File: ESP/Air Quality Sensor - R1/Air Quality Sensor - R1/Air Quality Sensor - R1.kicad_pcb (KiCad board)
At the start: 2 copper layers, 101.6 x 76.2 mm, 27 parts, among them U1 SCD4X, U2 CCS811, U3 SGP40, U4 Sensair_Sunrise_006-0-0007, U5 MICS-VZ-89TE‎, U6 SCD30, U7 BME680

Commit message: Pile of uncommitted boards.
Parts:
- added C11: 0.1u, Capacitor_SMD:C_0603_1608Metric, F.Cu at (78.2, -53.6)
- added D1: LED, custom:CHIPLED_0603, F.Cu at (89.0, -3.00)
- added H1: MountingHole, MountingHole:MountingHole_3.2mm_M3_Pad_Via, F.Cu at (3.81, -78.7)
- added H2: MountingHole, MountingHole:MountingHole_3.2mm_M3_Pad_Via, F.Cu at (97.8, -78.7)
- added H3: MountingHole, MountingHole:MountingHole_3.2mm_M3_Pad_Via, F.Cu at (3.81, -3.81)
- added H4: MountingHole, MountingHole:MountingHole_3.2mm_M3_Pad_Via, F.Cu at (97.8, -3.81)
- added J1: Conn_01x05, Connector_JST:JST_XH_B3B-XH-AM_1x03_P2.50mm_Vertical, F.Cu at (59.7, -4.33)
- added J2: Conn_01x09, Connector_JST:JST_XH_B9B-XH-AM_1x09_P2.50mm_Vertical, F.Cu at (33.3, -4.45)
- added J3: Conn_01x05, Connector_JST:JST_XH_B5B-XH-AM_1x05_P2.50mm_Vertical, F.Cu at (71.2, -4.33)
- added J4: Conn_01x04, Connector_JST:JST_XH_B4B-XH-AM_1x04_P2.50mm_Vertical, F.Cu at (19.4, -4.45)
- added R10: 4.7K, Resistor_SMD:R_0603_1608Metric, F.Cu at (75.0, -13.4)
- added R11: 4.7K, Resistor_SMD:R_0603_1608Metric, F.Cu at (77.5, -13.4)
- added R12: 470R, Resistor_SMD:R_0603_1608Metric, F.Cu at (70.0, -13.5)
- added R13: 4.7K, Resistor_SMD:R_0603_1608Metric, F.Cu at (59.7, -30.5)
- added R14: 470R, Resistor_SMD:R_0603_1608Metric, F.Cu at (38.7, -11.4)
- added R6: 4.7K, Resistor_SMD:R_0603_1608Metric, F.Cu at (69.8, -30.8)
- added R7: 4.7K, Resistor_SMD:R_0603_1608Metric, F.Cu at (77.4, -30.8)
- added R8: 4.7K, Resistor_SMD:R_0603_1608Metric, F.Cu at (64.7, -30.8)
- added R9: 4.7K, Resistor_SMD:R_0603_1608Metric, F.Cu at (67.2, -30.8)
- added TP10: TestPoint_Small, Connector_Pin:Pin_D1.0mm_L10.0mm, F.Cu at (66.0, -74.9)
- added TP6: TestPoint_Small, Connector_Pin:Pin_D1.0mm_L10.0mm, F.Cu at (66.0, -64.8)
- added TP7: TestPoint_Small, Connector_Pin:Pin_D1.0mm_L10.0mm, F.Cu at (66.0, -69.8)
- added TP8: TestPoint_Small, Connector_Pin:Pin_D1.0mm_L10.0mm, F.Cu at (66.0, -54.6)
- added TP9: TestPoint_Small, Connector_Pin:Pin_D1.0mm_L10.0mm, F.Cu at (66.0, -59.7)
- added U8: ESP32-POE, custom:ESP32-POE, F.Cu at (101.6, -21.6)
- C2, C7: value 0.1u -> 1.0u
- C4, C9: value 1.0u -> 0.1u
- U1: value SCD4X -> CCS811; footprint Sensor_Gas:Sensirion_SCD4X_QFN-20_EP_10.1x10.1_Pitch1.25mm -> Package_LGA:AMS_LGA-10-1EP_2.7x4mm_P0.6mm
- U2: value CCS811 -> SGP40; footprint Package_LGA:AMS_LGA-10-1EP_2.7x4mm_P0.6mm -> Sensor_Gas:Sensirion_DFN-6-1EP_2.44x2.44mm_P0.8mm
- U3: value SGP40 -> SCD4X; footprint Sensor_Gas:Sensirion_DFN-6-1EP_2.44x2.44mm_P0.8mm -> Sensor_Gas:Sensirion_SCD4X_QFN-20_EP_10.1x10.1_Pitch1.25mm
- U5: value MICS-VZ-89TE‎ -> BME680; footprint Sensor_Gas:Telaire_MICS-VZ-89TE‎ -> Package_LGA:Bosch_LGA-8_3x3mm_P0.8mm_ClockwisePinNumbering
- U6: value SCD30 -> MICS-VZ-89TE‎; footprint Sensor_Gas:Sensiron_SCD30_Module -> Sensor_Gas:Telaire_MICS-VZ-89TE‎
- U7: value BME680 -> SCD30; footprint Package_LGA:Bosch_LGA-8_3x3mm_P0.8mm_ClockwisePinNumbering -> Sensor_Gas:Sensiron_SCD30_Module
- moved U5 262.0 mm to (6.99, -67.3), turned to 0 degrees
- moved R4 261.6 mm to (10.8, -69.3), turned to 180 degrees
- moved C6 259.6 mm to (5.33, -64.8), turned to 180 degrees
- moved R3 258.7 mm to (10.8, -66.3), turned to 180 degrees
- moved C5 256.4 mm to (8.37, -64.8), turned to 0 degrees
- moved C4 253.9 mm to (5.52, -57.7)
- moved U3 245.8 mm to (7.55, -50.9)
- moved C3 238.4 mm to (5.52, -44.0)
- moved TP3 220.6 mm to (42.5, -57.3)
- moved U7 220.6 mm to (40.6, -46.9)
- moved TP4 219.6 mm to (42.7, -61.0)
- moved C7 219.5 mm to (42.8, -48.3), turned to 0 degrees
- moved R5 217.7 mm to (42.8, -63.5), turned to 0 degrees
- moved R1 195.7 mm to (89.4, -45.0)
- moved U1 194.6 mm to (90.2, -48.3), turned to 90 degrees
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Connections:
- U1 pad 1: (no net) -> GND
- U1 pad 10: /SENS/SDA -> /SENS/SCL_2
- U1 pad 11: (no net) -> GND
- U1 pad 2: (no net) -> Net-(R1-Pad2)
- U1 pad 3: (no net) -> Net-(TP1-Pad1)
- U1 pad 4: (no net) -> Net-(U1-Pad4)
- U1 pad 5: (no net) -> Net-(U1-Pad4)
- U1 pad 6: GND -> +3V3
- U1 pad 7: +3V3 -> Net-(R2-Pad1)
- U1 pad 8: (no net) -> unconnected-(U1-Pad8)
- U1 pad 9: /SENS/SCL -> /SENS/SDA_2
- U2 pad 1: GND -> +3V3
- U2 pad 2: Net-(R1-Pad2) -> GND
- U2 pad 3: Net-(TP1-Pad1) -> /SENS/SDA_2
- U2 pad 4: Net-(U2-Pad4) -> unconnected-(U2-Pad4)
- U2 pad 5: Net-(U2-Pad4) -> +3V3
- U2 pad 6: +3V3 -> /SENS/SCL_2
- U2 pad 7: Net-(R2-Pad1) -> GND
- U3 pad 1: +3V3 -> (no net)
- U3 pad 2: GND -> (no net)
- U3 pad 3: /SENS/SDA -> (no net)
- U3 pad 4: unconnected-(U3-Pad4) -> (no net)
- U3 pad 5: +3V3 -> (no net)
- U3 pad 6: /SENS/SCL -> GND
- U3 pad 7: GND -> +3V3
- U4 pad 4: /SENS/SDA -> /SENS/SDA_1
- U4 pad 5: /SENS/SCL -> /SENS/SCL_1
- U4 pad 7: Net-(TP2-Pad1) -> Net-(TP5-Pad1)
- U5 pad 1: Net-(TP3-Pad1) -> GND
- U5 pad 2: /SENS/SCL -> Net-(R4-Pad2)
- U5 pad 3: GND -> /SENS/SDA_1
- U5 pad 4: /SENS/SDA -> /SENS/SCL_1
- U5 pad 5: unconnected-(U5-Pad5) -> Net-(R3-Pad2)
- U6 pad 1: +3V3 -> Net-(TP2-Pad1)
- U6 pad 2: GND -> /SENS/SCL_2
- U6 pad 3: /SENS/SCL -> GND
- U6 pad 4: /SENS/SDA -> /SENS/SDA_2
- U6 pad 5: Net-(TP4-Pad1) -> unconnected-(U6-Pad5)
- U6 pad 6: Net-(TP5-Pad1) -> +3V3
- U7 pad 1: GND -> +3V3
- U7 pad 2: Net-(R4-Pad2) -> GND
- U7 pad 3: /SENS/SDA -> /SENS/SCL_1
- U7 pad 4: /SENS/SCL -> /SENS/SDA_1
- U7 pad 5: Net-(R3-Pad2) -> Net-(TP3-Pad1)
- U7 pad 6: +3V3 -> Net-(TP4-Pad1)
- U7 pad 7: GND -> Net-(R5-Pad1)
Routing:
- net /SENS/SDA_1: track 0.00 -> 197.9 mm, vias 0 -> 3
- net /SENS/SCL_1: track 0.00 -> 186.9 mm, vias 0 -> 4
- net /SENS/SCL_2: track 0.00 -> 149.5 mm, vias 0 -> 4
- net /SENS/SDA_2: track 0.00 -> 134.1 mm
- net +5V: track 0.00 -> 81.7 mm, vias 0 -> 1
- net GND: track 0.00 -> 65.4 mm, vias 0 -> 20
- net Net-(J1-Pad2): track 0.00 -> 59.7 mm
- net Net-(R13-Pad1): track 0.00 -> 58.8 mm
- net +3V3: track 0.00 -> 55.3 mm, vias 0 -> 18
- net Net-(J2-Pad7): track 0.00 -> 54.8 mm, vias 0 -> 2
- net Net-(D1-Pad2): track 0.00 -> 32.6 mm
- net Net-(R14-Pad1): track 0.00 -> 17.7 mm
- net Net-(TP5-Pad1): track 0.00 -> 11.7 mm
- net Net-(J3-Pad3): track 0.00 -> 8.81 mm
- net Net-(J3-Pad4): track 0.00 -> 8.79 mm
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- added copper zone on In2.Cu, net +3V3
- added copper zone on In1.Cu, net GND
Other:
- board size 101.6 x 76.2 mm -> 101.6 x 82.5 mm
- copper layers 2 -> 4
- board text added: "GND"
- board text added: "SCL1"
- board text added: "SCL2"
- board text added: "SDA1"
- board text added: "SDA2"

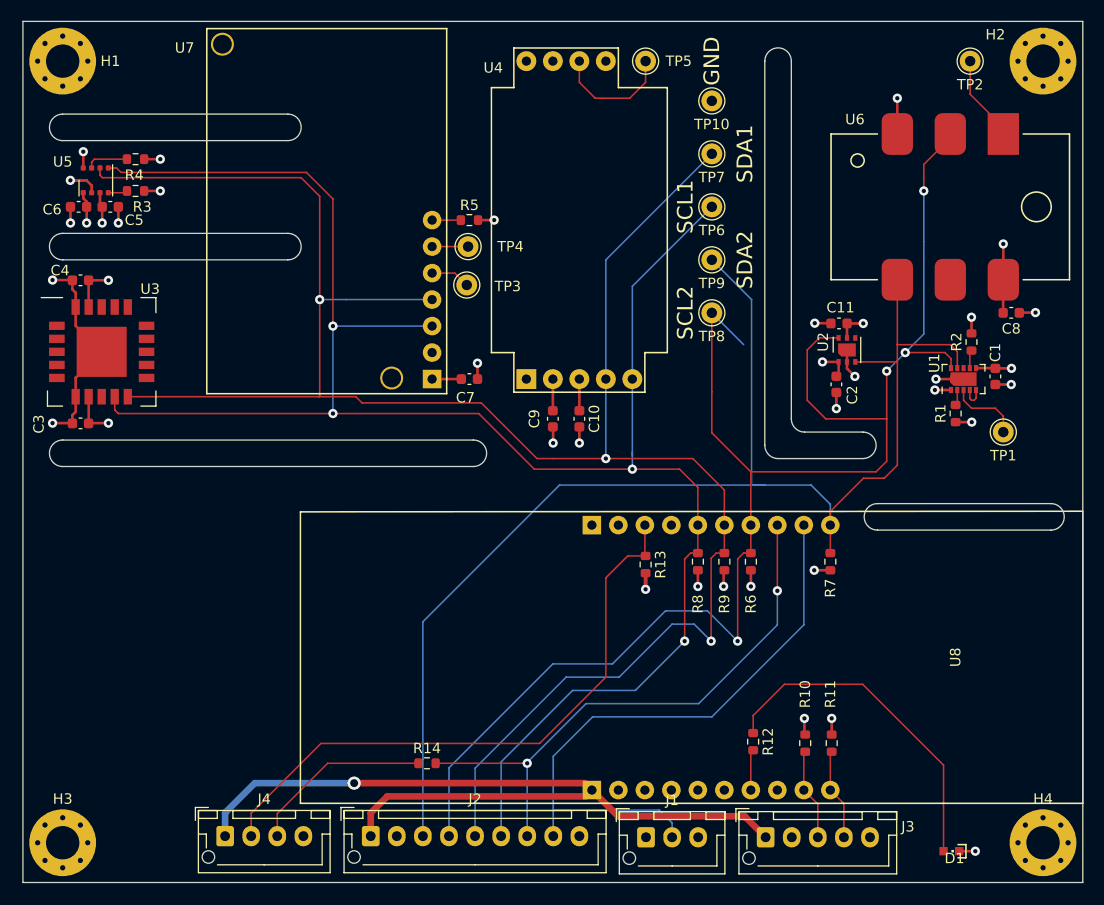
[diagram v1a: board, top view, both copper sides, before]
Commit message: Reworking things to use the new controller PCB.
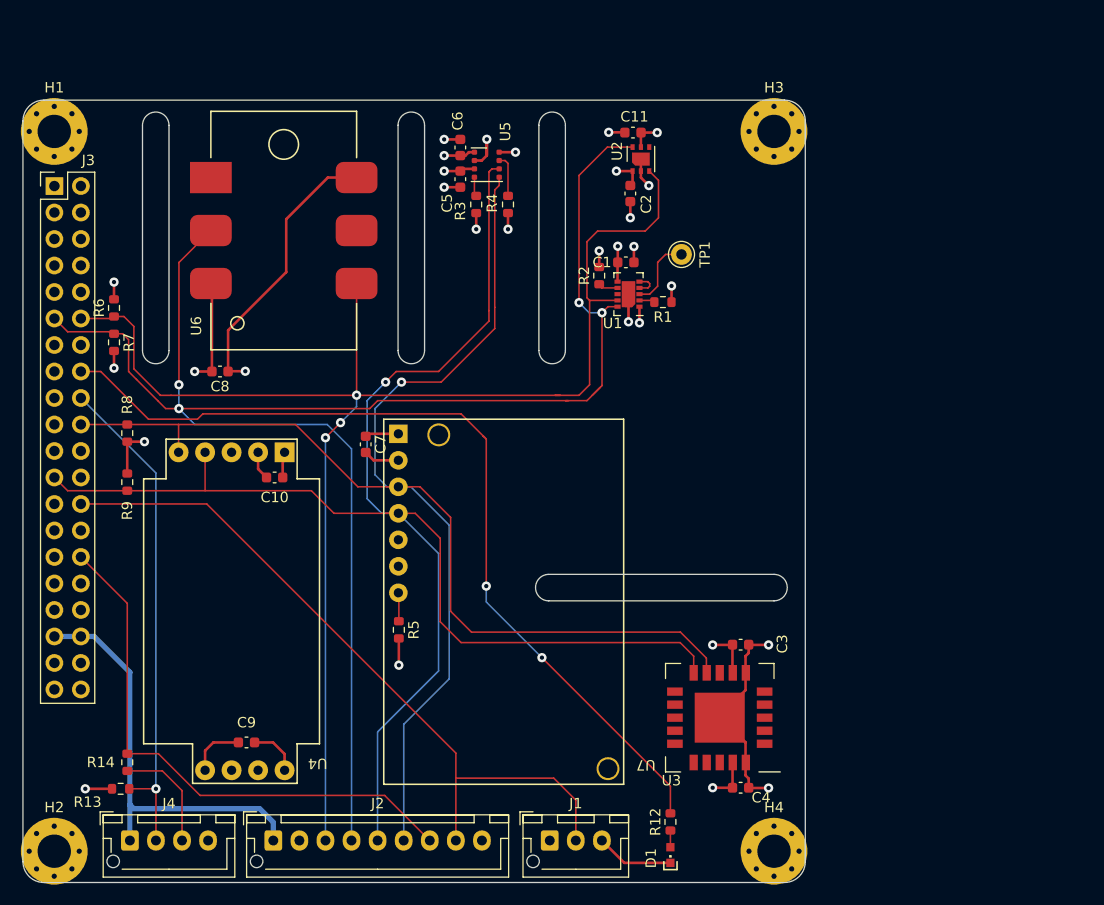
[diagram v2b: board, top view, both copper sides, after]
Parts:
- removed R10, R11: 4.7K, Resistor_SMD:R_0603_1608Metric
- removed TP10, TP2, TP3, TP4, TP5, TP6, TP7, TP8, TP9: TestPoint_Small, Connector_Pin:Pin_D1.0mm_L10.0mm
- removed U8: ESP32-POE, custom:ESP32-POE
- added ? (x2): , , F.Cu at (72.0, -72.0)
- added ?: , , F.Cu at (3.00, -72.0)
- J3: value Conn_01x05 -> ESP32-DevBoard-Header; footprint Connector_JST:JST_XH_B5B-XH-AM_1x05_P2.50mm_Vertical -> Connector_PinHeader_2.54mm:PinHeader_2x20_P2.54mm_Vertical
- moved H2 121.3 mm to (3.00, -3.00)
- moved H3 96.4 mm to (72.0, -72.0)
- moved J3 92.4 mm to (3.01, -66.8)
- moved C4 79.8 mm to (68.8, -9.08), turned to 0 degrees
- moved C8 76.1 mm to (18.9, -49.0), turned to 180 degrees
- moved R7 71.8 mm to (8.73, -51.8)
- moved U3 68.9 mm to (66.8, -15.8), turned to 180 degrees
- moved C3 66.7 mm to (68.8, -22.8), turned to 0 degrees
- moved R6 65.7 mm to (8.73, -55.1), turned to 90 degrees
- moved U6 63.9 mm to (25.0, -62.5), turned to 0 degrees
- moved R9 57.7 mm to (10.00, -38.4), turned to 90 degrees
- moved R8 56.1 mm to (10.00, -43.1)
- moved R13 54.7 mm to (9.36, -8.98), turned to 180 degrees
- moved C9 42.7 mm to (21.4, -13.4), turned to 180 degrees
- moved R5 39.9 mm to (36.0, -24.2), turned to -90 degrees
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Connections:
- J1 pad 2: Net-(J1-Pad2) -> Net-(J2-Pad8)
- J2 pad 8: Net-(J1-Pad2) -> Net-(J2-Pad8)
- J3 pad 1: +5V -> GND
- J3 pad 2: +3V3 -> GND
- J3 pad 3: Net-(J3-Pad3) -> +3V3
- J3 pad 4: Net-(J3-Pad4) -> +3V3
- R6 pad 1: /SENS/SCL_2 -> /SENS/SDA_2
- R7 pad 1: /SENS/SDA_2 -> /SENS/SCL_2
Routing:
- net GND: track 65.4 -> 194.4 mm, vias 20 -> 15
- net +3V3: track 55.3 -> 175.7 mm, vias 18 -> 15
- net Net-(R12-Pad2): track 3.91 -> 85.4 mm, vias 0 -> 2
- net Net-(J2-Pad8): track 0.00 -> 70.5 mm
- net Net-(J1-Pad2): track 59.7 -> 0.00 mm
- net /SENS/SDA_1: track 197.9 -> 157.0 mm, vias 3 -> 1
- net +5V: track 81.7 -> 41.0 mm, vias 1 -> 0
- net /SENS/SCL_1: track 186.9 -> 155.3 mm, vias 4 -> 1
- net Net-(D1-Pad2): track 32.6 -> 1.60 mm
- net /SENS/SCL_2: track 149.5 -> 164.0 mm
- net Net-(TP5-Pad1): track 11.7 -> 0.00 mm
- net Net-(R13-Pad1): track 58.8 -> 48.0 mm, vias 0 -> 1
- net Net-(J3-Pad3): track 8.81 -> 0.00 mm
- net Net-(J3-Pad4): track 8.79 -> 0.00 mm
- net Net-(TP2-Pad1): track 8.30 -> 0.00 mm
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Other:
- board size 101.6 x 82.5 mm -> 75 x 75 mm
- board text removed: "GND"
- board text removed: "SCL1"
- board text removed: "SCL2"
- board text removed: "SDA1"
- board text removed: "SDA2"

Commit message: Projects Projects Projects Projects.
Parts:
- removed ? (x3): , 
- added J5: Conn_01x09, Connector_Molex:Molex_PicoBlade_53047-0710_1x07_P1.25mm_Vertical, F.Cu at (69.9, -17.4)
- added R10: 4.7K, Resistor_SMD:R_0603_1608Metric, F.Cu at (64.5, -12.4)
- added R11: 4.7K, Resistor_SMD:R_0603_1608Metric, F.Cu at (64.5, -10.9)
- added TP10: TestPoint_Small, Connector_Pin:Pin_D1.0mm_L10.0mm, F.Cu at (3.01, -13.2)
- added TP2: TestPoint_Small, Connector_Pin:Pin_D1.0mm_L10.0mm, F.Cu at (8.98, -71.7)
- added TP3: TestPoint_Small, Connector_Pin:Pin_D1.0mm_L10.0mm, F.Cu at (32.2, -32.7)
- added TP4: TestPoint_Small, Connector_Pin:Pin_D1.0mm_L10.0mm, F.Cu at (32.2, -30.2)
- added TP5: TestPoint_Small, Connector_Pin:Pin_D1.0mm_L10.0mm, F.Cu at (31.8, -10.4)
- J1: footprint Connector_JST:JST_XH_B3B-XH-AM_1x03_P2.50mm_Vertical -> Connector_JST:JST_XH_B3B-XH-A_1x03_P2.50mm_Vertical
- J2: footprint Connector_JST:JST_XH_B9B-XH-AM_1x09_P2.50mm_Vertical -> Connector_JST:JST_XH_B9B-XH-A_1x09_P2.50mm_Vertical
- J4: footprint Connector_JST:JST_XH_B4B-XH-AM_1x04_P2.50mm_Vertical -> Connector_JST:JST_XH_B4B-XH-A_1x04_P2.50mm_Vertical
- moved C3 18.1 mm to (68.8, -40.9)
- moved C4 18.1 mm to (68.8, -27.2)
- moved U3 18.1 mm to (66.8, -33.9)
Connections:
- J1 pad 2: Net-(J2-Pad8) -> Net-(J1-Pad2)
- J2 pad 8: Net-(J2-Pad8) -> Net-(J1-Pad2)
- J3 pad 24: unconnected-(J3-Pad24) -> Net-(J1-Pad2)
- J3 pad 25: unconnected-(J3-Pad25) -> Net-(R10-Pad2)
- J3 pad 26: Net-(J2-Pad8) -> unconnected-(J3-Pad26)
- J3 pad 27: unconnected-(J3-Pad27) -> Net-(J3-Pad27)
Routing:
- net +5V: track 41.0 -> 132.0 mm
- net Net-(J1-Pad2): track 0.00 -> 78.0 mm, vias 0 -> 2
- net Net-(R10-Pad2): track 0.00 -> 70.5 mm
- net Net-(J2-Pad8): track 70.5 -> 0.00 mm
- net Net-(J3-Pad27): track 0.00 -> 70.1 mm
- net Net-(TP2-Pad1): track 0.00 -> 52.5 mm, vias 0 -> 1
- net Net-(TP5-Pad1): track 0.00 -> 13.7 mm
- net GND: track 194.4 -> 206.4 mm
- net /SENS/SCL_1: track 155.3 -> 146.0 mm
- net /SENS/SDA_1: track 157.0 -> 150.6 mm
- net Net-(J5-Pad6): track 0.00 -> 4.69 mm
- net Net-(J5-Pad5): track 0.00 -> 4.58 mm
- net Net-(TP4-Pad1): track 0.00 -> 3.81 mm
- net Net-(TP3-Pad1): track 0.00 -> 3.81 mm
- net +3V3: track 175.7 -> 174.5 mm
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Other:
- outline, holes or cut-outs redrawn

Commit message: Blerp.
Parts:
- added J6: Conn_01x08, Connector_Molex:Molex_PicoBlade_53047-0910_1x09_P1.25mm_Vertical, F.Cu at (63.2, -7.89)
- moved D1 59.6 mm to (3.01, -10.9)
- moved R12 59.6 mm to (3.01, -14.1)
- moved TP10 52.6 mm to (8.73, -65.5)
- moved R7 47.6 mm to (56.4, -50.4), turned to 0 degrees
- moved R6 47.6 mm to (55.6, -63.3)
- moved R11 9.07 mm to (62.7, -2.00)
- moved R10 8.69 mm to (62.7, -3.90)
- moved R9 7.50 mm to (17.5, -38.1), turned to -90 degrees
- moved R8 7.05 mm to (15.0, -38.1)
- moved TP2 1.80 mm to (8.73, -69.9)
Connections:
- J3 pad 13: unconnected-(J3-Pad13) -> Net-(J3-Pad13)
- J3 pad 14: unconnected-(J3-Pad14) -> Net-(J3-Pad14)
- J3 pad 15: unconnected-(J3-Pad15) -> Net-(J3-Pad15)
- J3 pad 17: unconnected-(J3-Pad17) -> Net-(J3-Pad17)
- J3 pad 19: unconnected-(J3-Pad19) -> Net-(J3-Pad19)
- J3 pad 26: unconnected-(J3-Pad26) -> Net-(J3-Pad26)
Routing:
- net Net-(J3-Pad13): track 0.00 -> 80.2 mm
- net Net-(J3-Pad15): track 0.00 -> 78.7 mm
- net Net-(J3-Pad14): track 0.00 -> 77.4 mm
- net Net-(J3-Pad17): track 0.00 -> 77.2 mm
- net Net-(J3-Pad19): track 0.00 -> 75.6 mm
- net Net-(J3-Pad26): track 0.00 -> 68.3 mm
- net Net-(J3-Pad16): track 85.2 -> 40.2 mm, vias 2 -> 0
- net Net-(J3-Pad18): track 48.0 -> 70.4 mm
- net +3V3: track 174.5 -> 192.6 mm, vias 15 -> 13
- net Net-(J5-Pad6): track 4.69 -> 13.5 mm
- net Net-(J5-Pad5): track 4.58 -> 12.5 mm
- net Net-(J1-Pad2): track 78.0 -> 73.1 mm, vias 2 -> 1
- net /SENS/SCL_1: track 146.0 -> 149.4 mm
- net GND: track 206.4 -> 203.3 mm, vias 15 -> 16
- net Net-(J3-Pad27): track 70.1 -> 72.0 mm
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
